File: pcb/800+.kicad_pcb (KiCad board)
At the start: 2 copper layers, 50.5 x 195.6 mm, 175 parts, among them J1 2inch LCD, J2 USB_B_Micro, J3 MSP_SBW, J4 Battery, J5 Cradle, J6 ESP_JTAG, J7 ESP_PROG, Q1 AO3401A, Q2 AO3401A, Q3 AO3401A, Q4 AO3401A, SW1 Off, SW10 R_LCD3, SW11 R_LCD4, SW12 LCD_LEFT, SW13 LCD_RIGHT, SW14 Glow, SW15 Device, SW16 Media, SW17 Mute, SW18 Prev, SW19 Vol+, SW2 Activities, SW20 Vol-, SW21 Ch+, SW22 Ch-, SW23 Dpad_Up, SW24 Dpad_Left, SW25 Dpad_Right, SW26 Dpad_Down, SW27 Dpad_OK, SW28 PgUp/Grn, SW29 PgDown/Yel, SW3 Help, SW30 Menu, SW31 Exit, SW32 Guide, SW33 Info, SW34 Stop, SW35 Replay, SW36 Skip, SW37 Play, SW38 Rec, SW39 Rew, SW4 L_LCD1, SW40 Fwd, SW41 Pause, SW42 KP_1, SW43 KP_2, SW44 KP_3, SW45 KP_4, SW46 KP_5, SW47 KP_6, SW48 KP_7, SW49 KP_8, SW5 L_LCD2, SW50 KP_9, SW51 KP_0, SW52 KP_Clear, SW53 KP_Enter, SW54 Red, SW55 Blue, SW56 SW_RollingBall, SW6 L_LCD3, SW7 L_LCD4, SW8 R_LCD1, SW9 R_LCD2, U1 MSP430G2553IPW28, U10 MAX17048, U11 MCP73831, U12 VEML7700-TR, U2 ESP32-S3-WROOM-1U, U3 USBLC6-2, U4 RT9080-3.3, U5 LM66200DRLR, U6 LM66200DRLR, U7 TSOP75340TT, U8 SPX3819M5-L, U9 RT9080-3.3

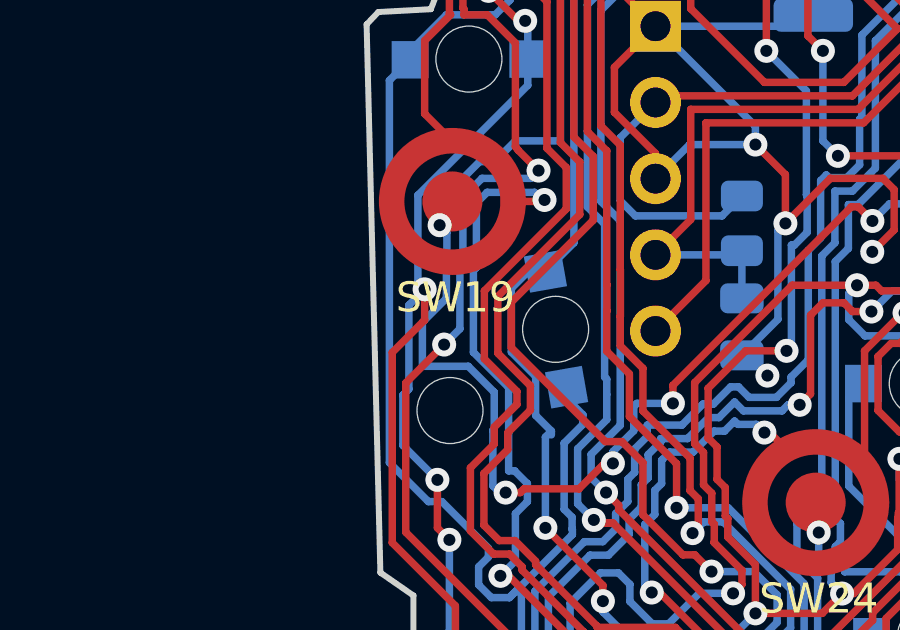
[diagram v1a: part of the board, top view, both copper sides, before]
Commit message: update case screws
bottom courtyard added for case screws to account for boss on the case
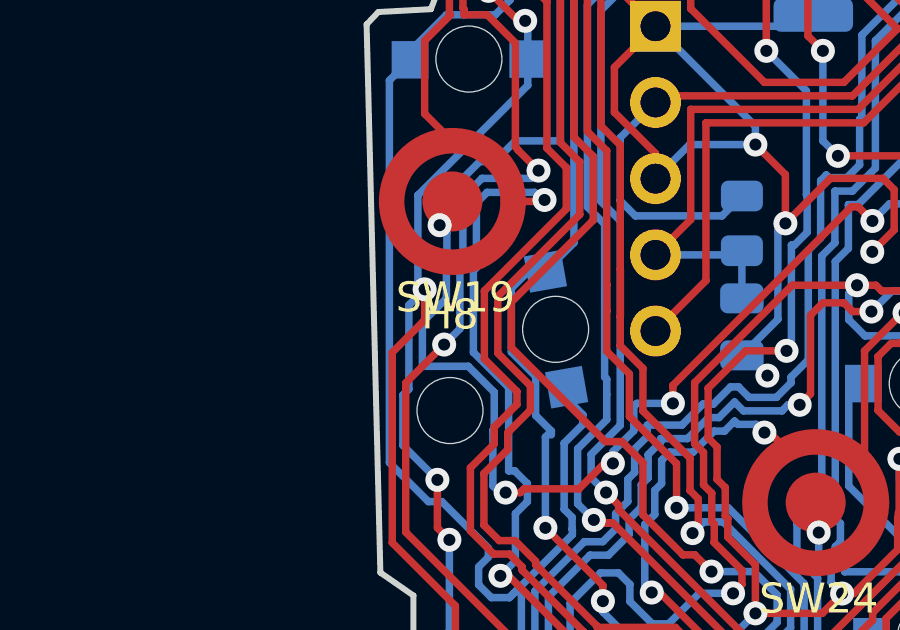
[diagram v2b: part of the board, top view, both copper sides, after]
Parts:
- H6, H9: footprint MountingHole:MountingHole_2.2mm_M2 -> 880+:MountingHole_Boss
- H7, H8: value Case Screw -> PCB Screw
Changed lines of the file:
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@@
     (grid_origin 91.45 137.3)
     (pcbplotparams
-      (layerselection 0x00010fc_ffffffff)
+      (layerselection 0x0000080_7ffffffe)
       (plot_on_all_layers_selection 0x0001000_00000000)
       (disableapertmacros false)
@@
     (property "ki_keywords" "mounting hole")
     (attr exclude_from_pos_files)
-    (fp_text reference "H8" (at 0 -3.2) (layer "F.SilkS") hide
-        (effects (font (size 1 1) (thickness 0.15)))
-    )
-    (fp_text value "Case Screw" (at 0 3.2) (layer "F.Fab")
-        (effects (font (size 1 1) (thickness 0.15)))
-    )
-    (fp_text user "${REFERENCE}" (at 0.3 0) (layer "F.Fab")
+    (fp_text reference "H8" (at 0 -3.2) (layer "F.SilkS")
+        (effects (font (size 1 1) (thickness 0.15)))
+    )
+    (fp_text value "PCB Screw" (at 0 3.2) (layer "F.Fab")
+        (effects (font (size 1 1) (thickness 0.15)))
+    )
+    (fp_text user "${REFERENCE}" (at 0 0) (layer "F.Fab")
         (effects (font (size 1 1) (thickness 0.15)))
     )
@@
         (effects (font (size 1 1) (thickness 0.15)))
     )
-    (fp_text value "Case Screw" (at 0 3.2) (layer "F.Fab")
+    (fp_text value "PCB Screw" (at 0 3.2) (layer "F.Fab")
         (effects (font (size 1 1) (thickness 0.15)))
     )
@@
       ))
   )
-  (footprint "MountingHole:MountingHole_2.2mm_M2" locked (layer "F.Cu")
+  (footprint "880+:MountingHole_Boss" locked (layer "F.Cu")
     (at 101.6 226.1)
     (descr "Mounting Hole 2.2mm, no annular, M2")
@@
     (fp_circle (center 0 0) (end 2.2 0)
       (stroke (width 0.15) (type solid)) (fill none) (layer "Cmts.User"))
-    (fp_circle (center 0 0) (end 2.45 0)
+    (fp_circle (center 0 0) (end 3.75 0)
+      (stroke (width 0.05) (type solid)) (fill none) (layer "B.CrtYd"))
+    (fp_circle (center 0 0) (end 3.75 0)
       (stroke (width 0.05) (type solid)) (fill none) (layer "F.CrtYd"))
     (pad "" np_thru_hole circle locked (at 0 0) (size 2.2 2.2) (drill 2.2) (layers "*.Cu" "*.Mask"))
@@
       ))
   )
-  (footprint "MountingHole:MountingHole_2.2mm_M2" locked (layer "F.Cu")
+  (footprint "880+:MountingHole_Boss" locked (layer "F.Cu")
     (at 101.62 52.88)
     (descr "Mounting Hole 2.2mm, no annular, M2")
@@
     (fp_circle (center 0 0) (end 2.2 0)
       (stroke (width 0.15) (type solid)) (fill none) (layer "Cmts.User"))
-    (fp_circle (center 0 0) (end 2.45 0)
+    (fp_circle (center 0 0) (end 3.75 0)
+      (stroke (width 0.05) (type solid)) (fill none) (layer "B.CrtYd"))
+    (fp_circle (center 0 0) (end 3.75 0)
       (stroke (width 0.05) (type solid)) (fill none) (layer "F.CrtYd"))
     (pad "" np_thru_hole circle locked (at 0 0) (size 2.2 2.2) (drill 2.2) (layers "*.Cu" "*.Mask"))
